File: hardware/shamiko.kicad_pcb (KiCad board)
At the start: 6 copper layers, 150 x 150 mm, 515 parts, among them IC1 LT3071, IC2 LT3071, IC3 MCP1727-ADJE_MF, IC4 MCP1727-ADJE_MF, IC5 MCP1727-ADJE_MF, IC6 FT2232HL-TRAY, IC7 AT93C46DN-SH-B, IC8 LT1763CS8-5#PBF, J1 Jack-DC, J10 SMA, J11 SMA, J12 SMA, J13 SMA, J2 SMA, J3 SMA, J4 JTAG_CONFIG, J5 JTAG_CONFIG, J6 PIN_Socket_2x20, J7 Conn_02x08, J8 692221030100, J9 SMA, P1 USB_C_Plug_USB2.0, SW1 SW_DIP_x03, SW10 SW_DIP_x08, SW11 SW_MEC_5E, SW12 SW_MEC_5E, SW13 SW_MEC_5E, SW14 SW_MEC_5E, SW2 SW_DIP_x03, SW3 SW_MEC_5E, SW4 SW_MEC_5E, SW5 SW_MEC_5E, SW6 SW_MEC_5E, SW7 SW_DIP_x08, SW8 SW_MEC_5E, SW9 SW_MEC_5E, U1 LT8625SPJV-1#TRMPBF, U10 SN74LVC2G17DCKRE4, U11 LM2937IMP-3.3, U12 LM2937IMP-3.3, U13 FT600, U14 AD8000, U2 LT8625SPJV-1#TRMPBF, U3 XC7S100-2FGGA484I, U4 XC7S25-1CSGA225C, U5 IS25LP064A-JLLE, U6 SN74LVC2G17DCKRE4, U7 SN74LVC2G17DCKRE4, U8 IS25LP064A-JLLE, U9 SN74LVC2G17DCKRE4, Y1 12Mhz, Y2 30Mhz, Y3 HCI 1532P-48.000KWVDT, Y4 HCI 1532P-48.000KWVDT

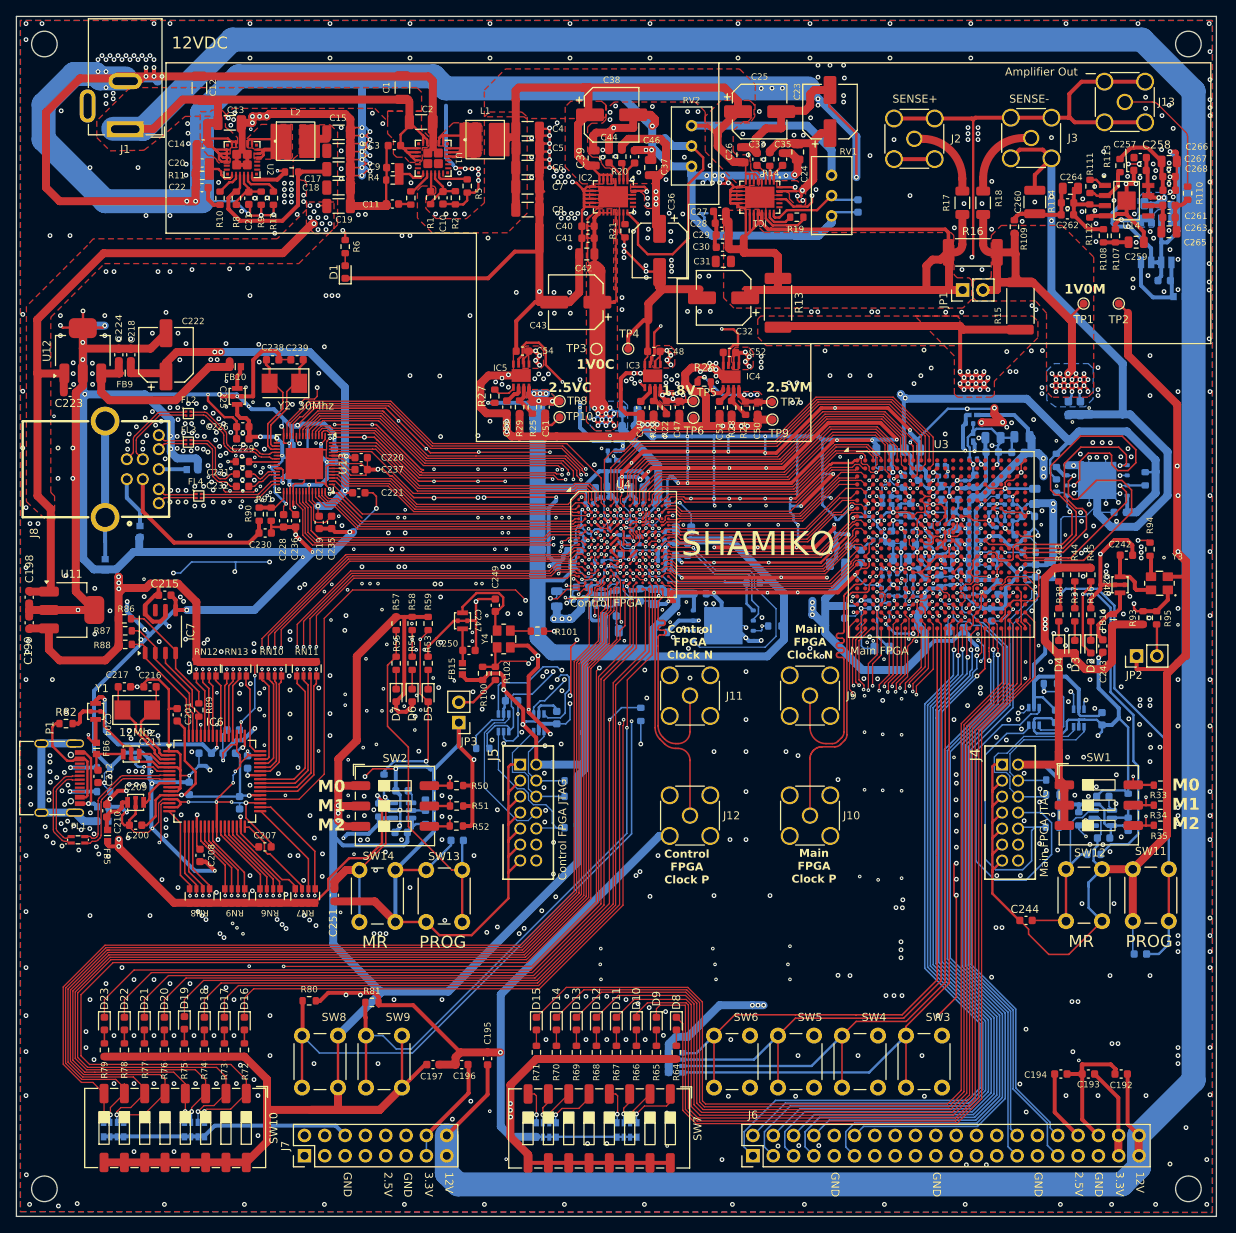
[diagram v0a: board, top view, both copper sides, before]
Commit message: Update hardware design and include board logo
Sync the saved schematics, PCB, project settings, and referenced custom
libraries with the updated design. Include the LOGO footprint and register
it in the project footprint table. The board now contains 524 footprints.

Keep unused source libraries, autosaves, backups, analysis outputs, and
manufacturing files out of the import. Point BOM exports to the existing
ignored production directory instead of a workstation-specific location.

Validation with KiCad 9.0.1:
- Netlist export succeeds and referenced custom libraries resolve.
- DRC: 0 errors, 40 warnings, 0 unconnected items, 0 schematic mismatches.
- ERC: 27 errors and 71 warnings, identical to the source design.

The pre-existing missing JTAG 3D model (87831-1420.stp) is not supplied by
the source project and remains unresolved.
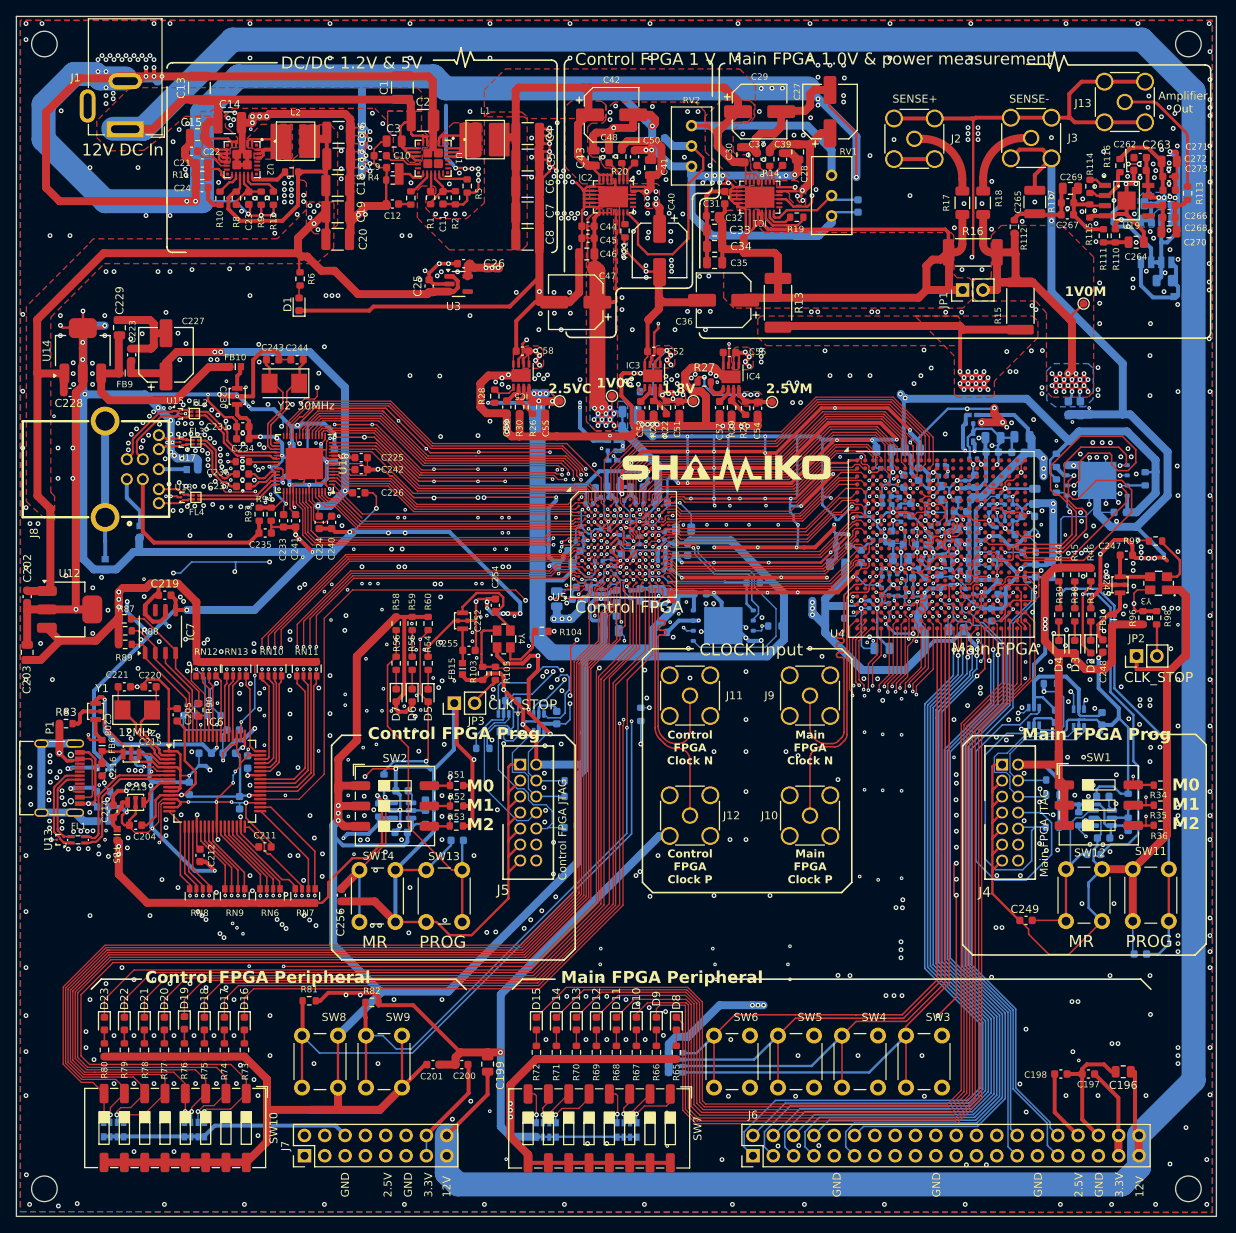
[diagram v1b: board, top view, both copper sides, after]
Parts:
- removed TP10, TP6, TP9: TestPoint, TestPoint:TestPoint_Pad_D1.0mm
- removed the TP2 at (158.6, 61.0)
- removed the TP4 at (97.3, 66.7)
- added C10: 1u, Capacitor_SMD:C_0603_1608Metric, F.Cu at (66.3, 42.5)
- added C22: 1u, Capacitor_SMD:C_0603_1608Metric, F.Cu at (42.7, 42.0)
- added C222: 0.1u, Capacitor_SMD:C_0603_1608Metric, B.Cu at (44.2, 111.0)
- added C25: 1u, Capacitor_SMD:C_0603_1608Metric, F.Cu at (72.4, 58.8)
- added C26: 1u, Capacitor_SMD:C_0603_1608Metric, F.Cu at (76.7, 56.0)
- added G***: LOGO, LOGO:logo, F.Cu at (109.6, 81.7)
- added R23: 100k, Resistor_SMD:R_0603_1608Metric, B.Cu at (99.6, 72.0)
- added R91: 4.7k, Resistor_SMD:R_0603_1608Metric, B.Cu at (45.5, 112.5)
- added R92: 10k, Resistor_SMD:R_0603_1608Metric, B.Cu at (42.5, 112.5)
- added U13: TPD2EUSB30, Package_TO_SOT_SMD:Texas_DRT-3, F.Cu at (26.3, 128.0)
- added U15: TPD2EUSB30, Package_TO_SOT_SMD:Texas_DRT-3, F.Cu at (41.0, 74.8)
- added U17: TPD2EUSB30, Package_TO_SOT_SMD:Texas_DRT-3, F.Cu at (41.7, 78.3)
- added U18: TPD2EUSB30, Package_TO_SOT_SMD:Texas_DRT-3, F.Cu at (41.8, 85.2)
- added U3: TI LP2985-33DBVR, Package_TO_SOT_SMD:SOT-23-5, F.Cu at (76.1, 58.5)
- C1, C2, C4, C5, C6, C7, C8: footprint Capacitor_SMD:C_1206_3216Metric -> Capacitor_SMD:C_1210_3225Metric
- C13: renamed from C12; footprint Capacitor_SMD:C_1206_3216Metric -> Capacitor_SMD:C_1210_3225Metric
- C14: renamed from C13; footprint Capacitor_SMD:C_1206_3216Metric -> Capacitor_SMD:C_1210_3225Metric
- C15: renamed from C14; footprint Capacitor_SMD:C_0603_1608Metric -> Capacitor_SMD:C_0805_2012Metric
- C16: renamed from C15; footprint Capacitor_SMD:C_1206_3216Metric -> Capacitor_SMD:C_1210_3225Metric
- C17: renamed from C16; footprint Capacitor_SMD:C_1206_3216Metric -> Capacitor_SMD:C_1210_3225Metric
- C18: renamed from C17; footprint Capacitor_SMD:C_1206_3216Metric -> Capacitor_SMD:C_1210_3225Metric
- C19: renamed from C18; footprint Capacitor_SMD:C_1206_3216Metric -> Capacitor_SMD:C_1210_3225Metric
- C196: renamed from C192; footprint Capacitor_SMD:C_0603_1608Metric -> Capacitor_SMD:C_0805_2012Metric
- C199: renamed from C195; footprint Capacitor_SMD:C_0603_1608Metric -> Capacitor_SMD:C_0805_2012Metric
- C20: renamed from C19; footprint Capacitor_SMD:C_1206_3216Metric -> Capacitor_SMD:C_1210_3225Metric
- C202: renamed from C198; value 1u -> 0.1u
- C203: renamed from C199; value 1u -> 47u; footprint Capacitor_SMD:C_0603_1608Metric -> Capacitor_SMD:C_0805_2012Metric
- C228: renamed from C223; value 1u -> 0.1u
- C229: renamed from C224; value 1u -> 10u; footprint Capacitor_SMD:C_0603_1608Metric -> Capacitor_SMD:C_0805_2012Metric
- C259: renamed from C254; footprint Capacitor_SMD:C_0603_1608Metric -> Capacitor_SMD:C_0805_2012Metric
- C265: renamed from C260; value 1000p -> 1n
- C266: renamed from C261; value 1000p -> 1n
- C273: renamed from C268; value 1000p -> 1n
- C3: footprint Capacitor_SMD:C_0603_1608Metric -> Capacitor_SMD:C_0805_2012Metric
- C33: renamed from C29; footprint Capacitor_SMD:C_0603_1608Metric -> Capacitor_SMD:C_0805_2012Metric
- C34: renamed from C30; footprint Capacitor_SMD:C_0603_1608Metric -> Capacitor_SMD:C_0805_2012Metric
- C39: renamed from C35; value 1u -> 1n
- C50: renamed from C46; value 1u -> 1n
- C53: renamed from C49; value 4700 pF -> 4.7n
- C57: renamed from C53; value 4700 pF -> 4.7n
- C59: renamed from C55; value 4700 pF -> 4.7n
- D2, D5: value G_LED -> B_LED
- R11: value 33.2k -> 49.9k
- R117: renamed from R114; value 61.9 -> 62
- R25: renamed from R24; value 261k -> 357k
- R26: renamed from R25; value 91k -> 357k
- R30: renamed from R29; value 13k -> 51k
- Y1: value 12Mhz -> 12MHz
- Y2: value 30Mhz -> 30MHz
- Y3, Y4: value HCI 1532P-48.000KWVDT -> HCI 1532H-48.000GWVATS
- moved D1 7.04 mm to (56.1, 61.1)
- moved R6 6.94 mm to (56.3, 57.9)
- moved TP2 6.18 mm to (95.2, 72.5)
- moved C20 4.16 mm to (61.0, 53.0)
- moved C8 3.71 mm to (84.7, 53.0)
- moved C203 3.71 mm to (22.1, 104.6)
- moved C229 3.39 mm to (33.7, 64.0)
- moved C7 3.26 mm to (84.7, 49.7)
- moved C19 3.03 mm to (61.0, 49.5)
- moved C6 2.35 mm to (84.7, 46.4)
- moved C18 2.03 mm to (61.0, 46.2)
- moved C31 1.84 mm to (109.3, 47.8), turned to 90 degrees
- moved C5 1.50 mm to (84.7, 43.1)
- moved C32 1.43 mm to (107.8, 50.0)
- moved C15 1.37 mm to (43.4, 39.9)
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- renumbered C96 to C100, C97 to C101, C98 to C102, C99 to C103, C100 to C104, C101 to C105, C102 to C106, C103 to C107, C104 to C108, C105 to C109, C10 to C11, C106 to C110, C107 to C111, C108 to C112, C109 to C113, C110 to C114, C111 to C115, C112 to C116, C113 to C117, C114 to C118, C115 to C119, C11 to C12, C116 to C120, C117 to C121, C118 to C122, C119 to C123, C120 to C124, C121 to C125, C122 to C126, C123 to C127, C124 to C128, C125 to C129, C126 to C130, C127 to C131, C128 to C132, C129 to C133, C130 to C134, C131 to C135, C132 to C136, C133 to C137, C134 to C138, C135 to C139, C136 to C140, C137 to C141, C138 to C142, C139 to C143, C140 to C144, C141 to C145, C142 to C146, C143 to C147, C144 to C148, C145 to C149, C146 to C150, C147 to C151, C148 to C152, C149 to C153, C150 to C154, C151 to C155, C152 to C156, C153 to C157, C154 to C158, C155 to C159, C156 to C160, C157 to C161, C158 to C162, C159 to C163, C160 to C164, C161 to C165, C162 to C166, C163 to C167, C164 to C168, C165 to C169, C166 to C170, C167 to C171, C168 to C172, C169 to C173, C170 to C174, C171 to C175, C172 to C176, C173 to C177, C174 to C178, C175 to C179, C176 to C180, C177 to C181, C178 to C182, C179 to C183, C180 to C184, C181 to C185, C182 to C186, C183 to C187, C184 to C188, C185 to C189, C186 to C190, C187 to C191, C188 to C192, C189 to C193, C190 to C194, C191 to C195, C193 to C197, C194 to C198, C196 to C200, C197 to C201, C200 to C204, C201 to C205, C202 to C206, C203 to C207, C204 to C208, C205 to C209, C20 to C21, C206 to C210, C207 to C211, C208 to C212, C209 to C213, C210 to C214, C211 to C215, C212 to C216, C213 to C217, C214 to C218, C215 to C219, C216 to C220, C217 to C221, C218 to C223, C219 to C224, C220 to C225, C221 to C226, C222 to C227, C21 to C23, C225 to C230, C226 to C231, C227 to C232, C228 to C233, C229 to C234, C230 to C235, C231 to C236, C232 to C237, C233 to C238, C234 to C239, C22 to C24, C235 to C240, C236 to C241, C237 to C242, C238 to C243, C239 to C244, C240 to C245, C241 to C246, C242 to C247, C243 to C248, C244 to C249, C245 to C250, C246 to C251, C247 to C252, C248 to C253, C249 to C254, C250 to C255, C251 to C256, C252 to C257, C253 to C258, C255 to C260, C256 to C261, C257 to C262, C258 to C263, C259 to C264, C262 to C267, C263 to C268, C264 to C269, C23 to C27, C265 to C270, C266 to C271, C267 to C272, C24 to C28, C25 to C29, C26 to C30, C27 to C31, C28 to C32, C31 to C35, C32 to C36, C33 to C37, C34 to C38, C36 to C40, C37 to C41, C38 to C42, C39 to C43, C40 to C44, C41 to C45, C42 to C46, C43 to C47, C44 to C48, C45 to C49, C47 to C51, C48 to C52, C50 to C54, C51 to C55, C52 to C56, C54 to C58, C56 to C60, C57 to C61, C58 to C62, C59 to C63, C60 to C64, C61 to C65, C62 to C66, C63 to C67, C64 to C68, C65 to C69, C66 to C70, C67 to C71, C68 to C72, C69 to C73, C70 to C74, C71 to C75, C72 to C76, C73 to C77, C74 to C78, C75 to C79, C76 to C80, C77 to C81, C78 to C82, C79 to C83, C80 to C84, C81 to C85, C82 to C86, C83 to C87, C84 to C88, C85 to C89, C86 to C90, C87 to C91, C88 to C92, C89 to C93, C90 to C94, C91 to C95, C92 to C96, C93 to C97, C94 to C98, C95 to C99, R97 to R100, R98 to R101, R99 to R102, R100 to R103, R101 to R104, R102 to R105, R103 to R106, R104 to R107, R105 to R108, R106 to R109, R107 to R110, R108 to R111, R109 to R112, R110 to R113, R111 to R114, R112 to R115, R113 to R116, R23 to R24, R26 to R27, R27 to R28, R28 to R29, R30 to R31, R31 to R32, R32 to R33, R33 to R34, R34 to R35, R35 to R36, R36 to R37, R37 to R38, R38 to R39, R39 to R40, R40 to R41, R41 to R42, R42 to R43, R43 to R44, R44 to R45, R45 to R46, R46 to R47, R47 to R48, R48 to R49, R49 to R50, R50 to R51, R51 to R52, R52 to R53, R53 to R54, R54 to R55, R55 to R56, R56 to R57, R57 to R58, R58 to R59, R59 to R60, R60 to R61, R61 to R62, R62 to R63, R63 to R64, R64 to R65, R65 to R66, R66 to R67, R67 to R68, R68 to R69, R69 to R70, R70 to R71, R71 to R72, R72 to R73, R73 to R74, R74 to R75, R75 to R76, R76 to R77, R77 to R78, R78 to R79, R79 to R80, R80 to R81, R81 to R82, R82 to R83, R83 to R84, R84 to R85, R85 to R86, R86 to R87, R87 to R88, R88 to R89, R89 to R90, R90 to R93, R91 to R94, R92 to R95, R93 to R96, R94 to R97, R95 to R98, R96 to R99, TP3 to TP2, TP5 to TP3, TP7 to TP4, TP8 to TP5, U9 to U10, U10 to U11, U11 to U12, U12 to U14, U13 to U16, U14 to U19, U3 to U4, U4 to U5, U5 to U6, U6 to U7, U7 to U8, U8 to U9
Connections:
- C27 pad 1: +5V -> +3.3VP
- C28 pad 1: +5V -> +3.3VP
- C40 pad 1: +5V -> +3.3VP
- C41 pad 1: +5V -> +3.3VP
- IC1 pad 27: +5V -> +3.3VP
- IC1 pad 28: +5V -> +3.3VP
- IC2 pad 27: +5V -> +3.3VP
- IC2 pad 28: +5V -> +3.3VP
- R14 pad 1: +5V -> +3.3VP
- R20 pad 1: +5V -> +3.3VP
- R64 pad 1: C_LED_4 -> Net-(U5F-IO_L3P_T0_DQS_PUDC_B_14)
- RN12 pad 5: BCBUS7 -> unconnected-(RN12-Pad5)
- U1 pad 11: unconnected-(U1-INTVCC-Pad11) -> Net-(U1-INTVCC)
- U16 pad 14: GND -> unconnected-(U16-NC-Pad14)
- U2 pad 11: unconnected-(U2-INTVCC-Pad11) -> Net-(U2-INTVCC)
- U5 pad C4: FT600_CLK -> FT600_DATA_0
- U5 pad F4: FT600_DATA_0 -> FT600_CLK
- U5 pad K11: C_LED_4 -> Net-(U5F-IO_L3P_T0_DQS_PUDC_B_14)
- U5 pad P11: unconnected-(U4I-IO_L16N_T2_D31_14-PadP11) -> C_LED_4
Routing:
- net +3.3VP: track 0.00 -> 94.6 mm, vias 0 -> 13
- net +3.3V: track 249.0 -> 168.1 mm
- net GND: track 5255.1 -> 5334.2 mm, vias 1395 -> 1437
- net +5V: track 541.3 -> 480.9 mm, vias 34 -> 18
- net Net-(U5F-IO_L3P_T0_DQS_PUDC_B_14): track 0.00 -> 49.8 mm, vias 0 -> 2
- net C_LED_4: track 142.7 -> 104.6 mm, vias 2 -> 0
- net VBUS_FT323H: track 14.1 -> 45.7 mm, vias 0 -> 2
- net BCBUS7: track 65.1 -> 73.7 mm
- net ACBUS6_OE_B: track 125.3 -> 119.0 mm
- net Net-(IC1-OUT_1): track 105.1 -> 110.7 mm
- net Net-(Y4-OUTPUT): track 2.42 -> 7.04 mm
- net Net-(U2-INTVCC): track 0.00 -> 4.44 mm
- net Net-(U1-INTVCC): track 0.00 -> 4.37 mm
- net FT600_DATA_0: track 43.7 -> 48.1 mm
- net Net-(Y3-OUTPUT): track 2.87 -> 6.77 mm
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- added copper zone on F.Cu, net +3.3VP
- added copper zone on In4.Cu, net +3.3VP
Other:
- board text added: "12V DC In"
- board text added: "CLK_STOP"
- board text added: "CLOCK Input"
- board text added: "Control FPGA 1 V"
- board text added: "Control FPGA Peripheral"
- board text added: "Control FPGA Prog"
- board text added: "DC/DC 1.2V & 5V"
- board text added: "Main FPGA 1.0V & power measurement"
- board text added: "Main FPGA Peripheral"
- board text added: "Main FPGA Prog"
- board text removed: "12VDC"
- board text removed: "SHAMIKO"
